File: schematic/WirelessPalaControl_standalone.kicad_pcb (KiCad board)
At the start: 2 copper layers, 25.6 x 34.3 mm, 27 parts, among them J1 6P4C, J2 MCU UART, J3 WeMos_mini_Hat_Left, J4 WeMos_mini_Hat_Right, J5 RJ11 - Direct Link, Q1 AO3400A, Q2 AO3400A, U1 AMS1117-3.3

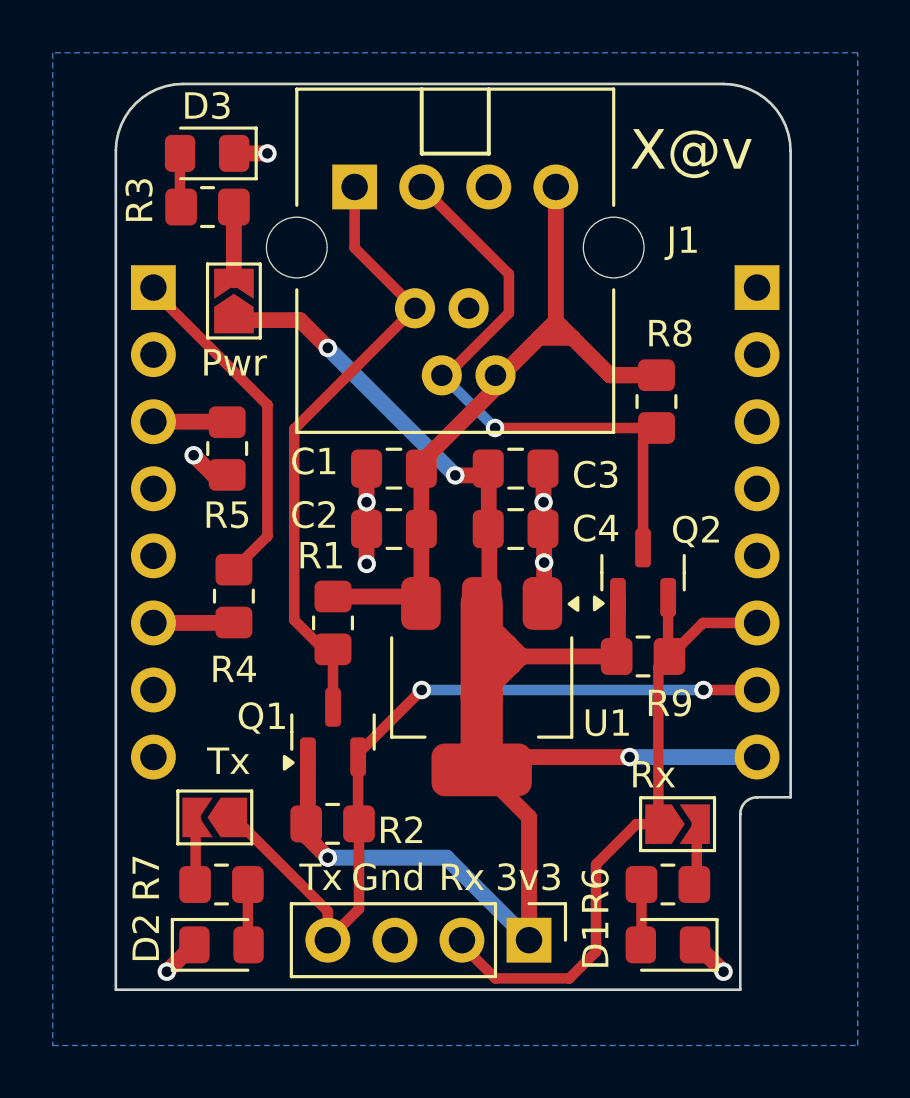
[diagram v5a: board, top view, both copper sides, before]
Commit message: feat(hw): draft - Use D1 mini LDO
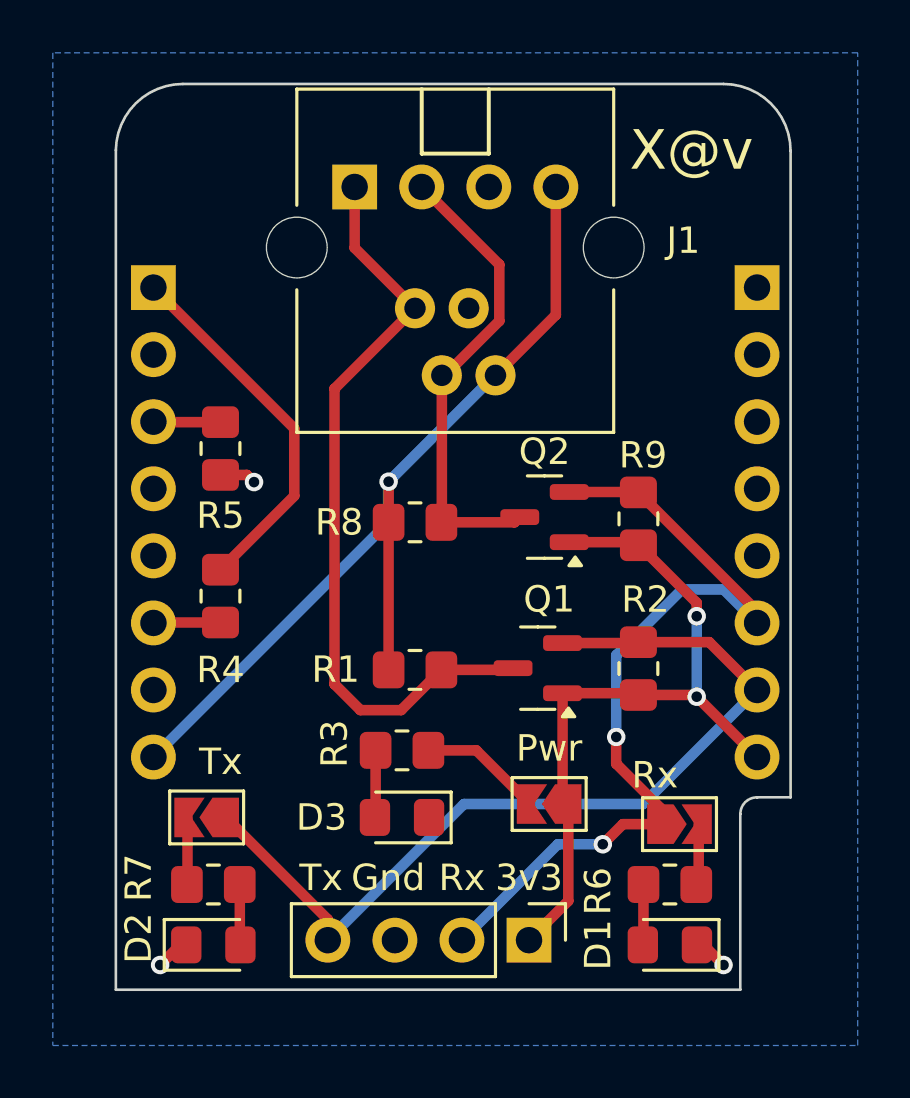
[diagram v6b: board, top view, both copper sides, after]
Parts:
- removed C1, C3: 10u, Capacitor_SMD:C_0805_2012Metric_Pad1.18x1.45mm_HandSolder
- removed C2, C4: 100n, Capacitor_SMD:C_0805_2012Metric_Pad1.18x1.45mm_HandSolder
- removed U1: AMS1117-3.3, Package_TO_SOT_SMD:SOT-223-3_TabPin2
- moved D3 26.2 mm to (33.5, 51.8)
- moved JP3 22.5 mm to (39.1, 51.3), turned to 180 degrees
- moved R3 21.9 mm to (33.5, 49.3)
- moved R2 13.0 mm to (42.5, 46.2), turned to -90 degrees
- moved R8 10.2 mm to (34.0, 40.6), turned to 180 degrees
- moved Q1 8.12 mm to (38.7, 46.2), turned to 180 degrees
- moved R9 5.21 mm to (42.5, 40.5), turned to -90 degrees
- moved Q2 4.28 mm to (38.9, 40.4), turned to 180 degrees
- moved R1 3.58 mm to (34.0, 46.2), turned to 180 degrees
- moved R4 0.51 mm to (26.7, 43.4)
- moved D2 0.31 mm to (26.4, 56.6)
- moved R7 0.31 mm to (26.4, 54.4)
- moved JP2 0.31 mm to (26.1, 51.8)
- moved R5 0.25 mm to (26.7, 37.8)
- moved D1 0.07 mm to (43.7, 56.6)
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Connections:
- J3 pad 8: unconnected-(J3-5V-Pad8) -> +5V
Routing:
- net +3.3V: track 65.5 -> 27.8 mm, vias 4 -> 2
- net GND: track 14.2 -> 4.01 mm, vias 8 -> 3
- net RXuC: track 25.1 -> 32.7 mm, vias 0 -> 2
- net +5V: track 29.3 -> 35.0 mm, vias 0 -> 1
- net Tx: track 23.1 -> 28.9 mm
- net Rx: track 23.4 -> 17.9 mm, vias 1 -> 0
- net TXuC: track 29.9 -> 34.6 mm, vias 2 -> 0
- net Net-(JP3-B): track 2.78 -> 4.69 mm
- net /GPIO1: track 13.0 -> 14.1 mm
- net /GPIO2: track 3.05 -> 2.55 mm
- net Net-(D3-A): track 2.05 -> 2.55 mm
